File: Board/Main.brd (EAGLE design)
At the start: 43.2 x 30.5 mm, 1 part

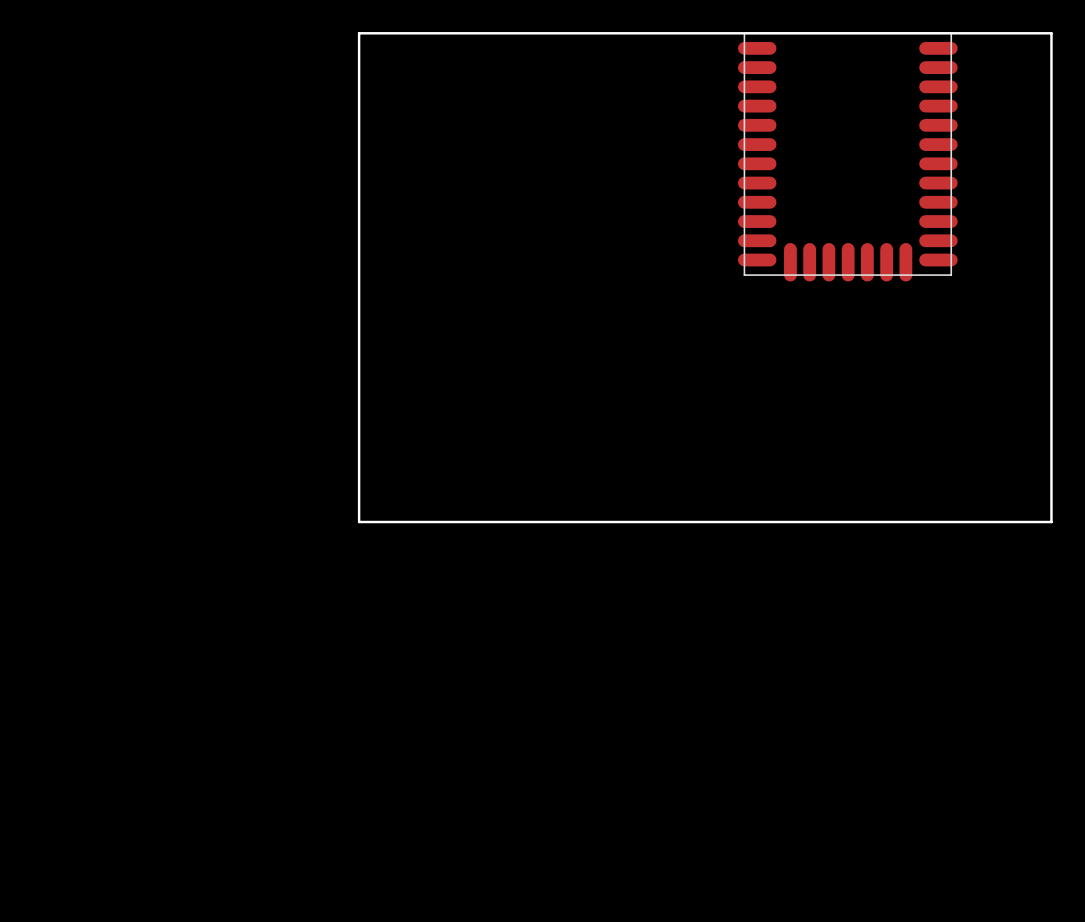
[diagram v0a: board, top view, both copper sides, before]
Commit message: Add battery managment
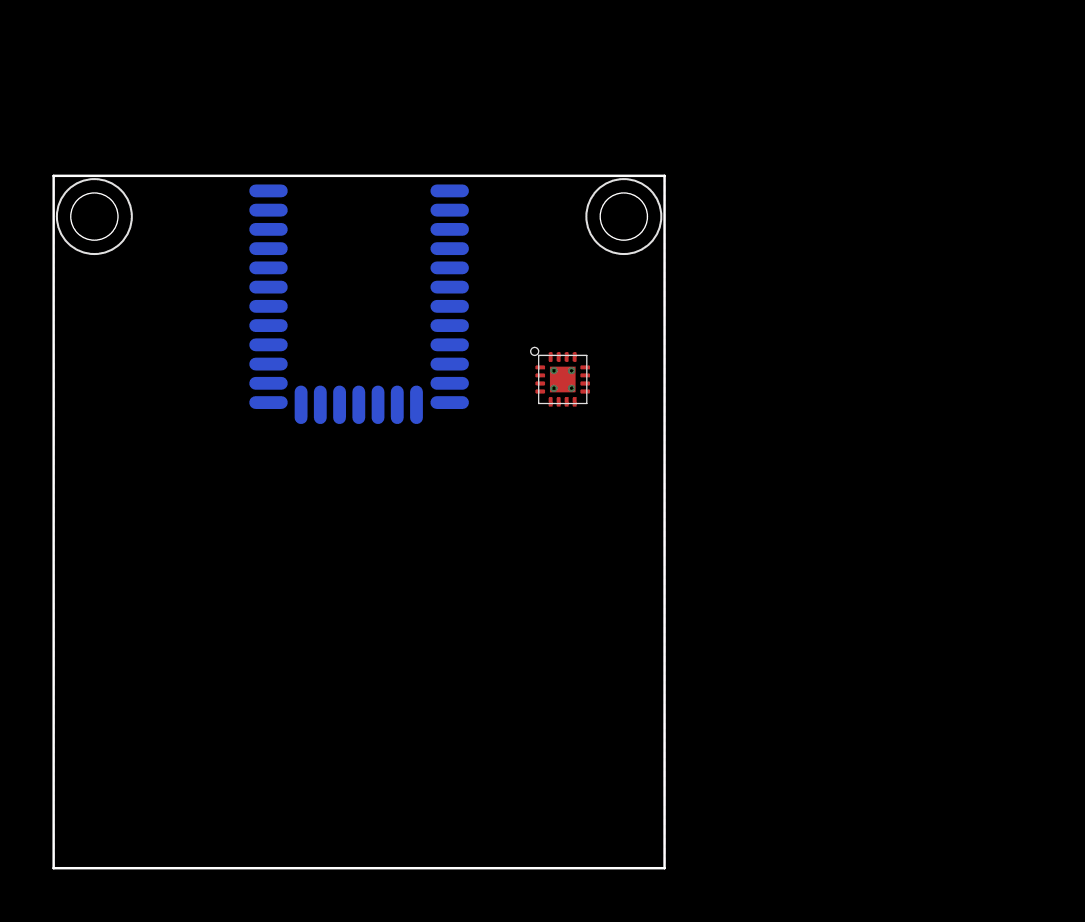
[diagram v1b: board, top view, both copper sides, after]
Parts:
- removed BGM111: BGM111, Main Components:BGM111
- added BLUETOOTH: BGM111, Main Components:BGM111
- added CHARGER: BQ24075, Main Components:VQFN-16
- added U$1, U$2: (no value), Hardware:#4_SCREW
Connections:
- new net +3V3: BLUETOOTH.VDD
- new net +5V0: CHARGER.13
- new net GND: BLUETOOTH.GND@0, BLUETOOTH.GND@1, BLUETOOTH.GND@2, BLUETOOTH.GND@3, CHARGER.15, CHARGER.17, CHARGER.17@1, CHARGER.17@2, CHARGER.17@3, CHARGER.17@4, CHARGER.4, CHARGER.8
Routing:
- added copper zone on layer 1, net GND
- added copper zone on layer 16, net GND
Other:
- board size 43.2 x 30.5 mm -> 38.1 x 43.2 mm
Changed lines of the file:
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@@
 <board>
 <plain>
-<wire x1="0" y1="0" x2="0" y2="30.48" width="0.1524" layer="20"/>
-<wire x1="0" y1="30.48" x2="43.18" y2="30.48" width="0.1524" layer="20"/>
-<wire x1="43.18" y1="30.48" x2="43.18" y2="0" width="0.1524" layer="20"/>
-<wire x1="43.18" y1="0" x2="0" y2="0" width="0.1524" layer="20"/>
+<wire x1="-19.05" y1="-21.59" x2="-19.05" y2="21.59" width="0.1524" layer="20"/>
+<wire x1="-19.05" y1="21.59" x2="19.05" y2="21.59" width="0.1524" layer="20"/>
+<wire x1="19.05" y1="21.59" x2="19.05" y2="-21.59" width="0.1524" layer="20"/>
+<wire x1="19.05" y1="-21.59" x2="-19.05" y2="-21.59" width="0.1524" layer="20"/>
 </plain>
 <attributes>
@@
 </class>
 </classes>
-<designrules name="default">
+<designrules name="OshPark *">
 <description language="de">&lt;b&gt;EAGLE Design Rules&lt;/b&gt;
 &lt;p&gt;
@@
 <param name="mdViaViaSameLayer" value="6mil"/>
 <param name="mnLayersViaInSmd" value="2"/>
-<param name="mdCopperDimension" value="40mil"/>
+<param name="mdCopperDimension" value="15mil"/>
 <param name="mdDrill" value="6mil"/>
 <param name="mdSmdStop" value="0mil"/>
 <param name="msWidth" value="6mil"/>
-<param name="msDrill" value="0.35mm"/>
-<param name="msMicroVia" value="9.99mm"/>
+<param name="msDrill" value="10mil"/>
+<param name="msMicroVia" value="10mil"/>
 <param name="msBlindViaRatio" value="0.5"/>
-<param name="rvPadTop" value="0.25"/>
-<param name="rvPadInner" value="0.25"/>
-<param name="rvPadBottom" value="0.25"/>
-<param name="rvViaOuter" value="0.25"/>
-<param name="rvViaInner" value="0.25"/>
+<param name="rvPadTop" value="0"/>
+<param name="rvPadInner" value="0"/>
+<param name="rvPadBottom" value="0"/>
+<param name="rvViaOuter" value="0"/>
+<param name="rvViaInner" value="0"/>
 <param name="rvMicroViaOuter" value="0.25"/>
 <param name="rvMicroViaInner" value="0.25"/>
-<param name="rlMinPadTop" value="10mil"/>
+<param name="rlMinPadTop" value="5mil"/>
 <param name="rlMaxPadTop" value="20mil"/>
-<param name="rlMinPadInner" value="10mil"/>
+<param name="rlMinPadInner" value="5mil"/>
 <param name="rlMaxPadInner" value="20mil"/>
-<param name="rlMinPadBottom" value="10mil"/>
+<param name="rlMinPadBottom" value="5mil"/>
 <param name="rlMaxPadBottom" value="20mil"/>
-<param name="rlMinViaOuter" value="8mil"/>
+<param name="rlMinViaOuter" value="5mil"/>
 <param name="rlMaxViaOuter" value="20mil"/>
-<param name="rlMinViaInner" value="8mil"/>
+<param name="rlMinViaInner" value="5mil"/>
 <param name="rlMaxViaInner" value="20mil"/>
 <param name="rlMinMicroViaOuter" value="4mil"/>
@@
 <param name="mvStopFrame" value="1"/>
 <param name="mvCreamFrame" value="0"/>
-<param name="mlMinStopFrame" value="4mil"/>
+<param name="mlMinStopFrame" value="2mil"/>
 <param name="mlMaxStopFrame" value="4mil"/>
 <param name="mlMinCreamFrame" value="0mil"/>
@@
 <param name="checkRestrict" value="1"/>
 <param name="checkStop" value="0"/>
-<param name="checkValues" value="0"/>
+<param name="checkValues" value="1"/>
 <param name="checkNames" value="1"/>
 <param name="checkWireStubs" value="1"/>
@@
 </autorouter>
 <elements>
-<element name="BGM111" library="Main Components" package="BGM111" value="BGM111" x="30.48" y="30.48" smashed="yes"/>
+<element name="CHARGER" library="Main Components" package="VQFN-16" value="BQ24075" x="12.7" y="8.89" smashed="yes">
+<attribute name="VALUE" value="BQ24075" x="12.7" y="8.89" size="1.778" layer="27" display="off"/>
+</element>
+<element name="BLUETOOTH" library="Main Components" package="BGM111" value="BGM111" x="0" y="21.59" smashed="yes" rot="MR0">
+<attribute name="NAME" x="1" y="13.59" size="1.27" layer="26" font="vector" rot="MR90" align="bottom-center"/>
+<attribute name="VALUE" x="-2" y="13.59" size="1.27" layer="28" font="vector" rot="MR90" align="bottom-center"/>
+</element>
+<element name="U$1" library="Hardware" package="#4_SCREW" value="" x="-16.51" y="19.05" smashed="yes"/>
+<element name="U$2" library="Hardware" package="#4_SCREW" value="" x="16.51" y="19.05" smashed="yes"/>
 </elements>
 <signals>
+<signal name="GND">
+<polygon width="0.1524" layer="1" isolate="0.4064">
+<vertex x="-19.05" y="21.59"/>
+<vertex x="19.05" y="21.59"/>
+<vertex x="19.05" y="-21.59"/>
+<vertex x="-19.05" y="-21.59"/>
+</polygon>
+<polygon width="0.1524" layer="16" isolate="0.4064">
+<vertex x="-19.05" y="21.59"/>
+<vertex x="19.05" y="21.59"/>
+<vertex x="19.05" y="-21.59"/>
+<vertex x="-19.05" y="-21.59"/>
+</polygon>
+<contactref element="BLUETOOTH" pad="GND@1"/>
+<contactref element="BLUETOOTH" pad="GND@3"/>
+<contactref element="BLUETOOTH" pad="GND@0"/>
+<contactref element="BLUETOOTH" pad="GND@2"/>
+<contactref element="CHARGER" pad="17@1"/>
+<contactref element="CHARGER" pad="8"/>
+<contactref element="CHARGER" pad="17@4"/>
+<contactref element="CHARGER" pad="17@3"/>
+<contactref element="CHARGER" pad="17"/>
+<contactref element="CHARGER" pad="17@2"/>
+<contactref element="CHARGER" pad="4"/>
+<contactref element="CHARGER" pad="15"/>
+<wire x1="12.15" y1="8.34" x2="12.7" y2="8.89" width="0" layer="19" extent="1-1"/>
+<wire x1="11.3" y1="8.14" x2="12.15" y2="8.34" width="0" layer="19" extent="1-1"/>
+<wire x1="13.45" y1="7.49" x2="13.25" y2="8.34" width="0" layer="19" extent="1-1"/>
+<wire x1="12.45" y1="10.29" x2="12.15" y2="9.44" width="0" layer="19" extent="1-1"/>
+</signal>
+<signal name="+3V3">
+<contactref element="BLUETOOTH" pad="VDD"/>
+</signal>
+<signal name="+5V0">
+<contactref element="CHARGER" pad="13"/>
+</signal>
 </signals>
 <mfgpreviewcolors>

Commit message: Add motor driver
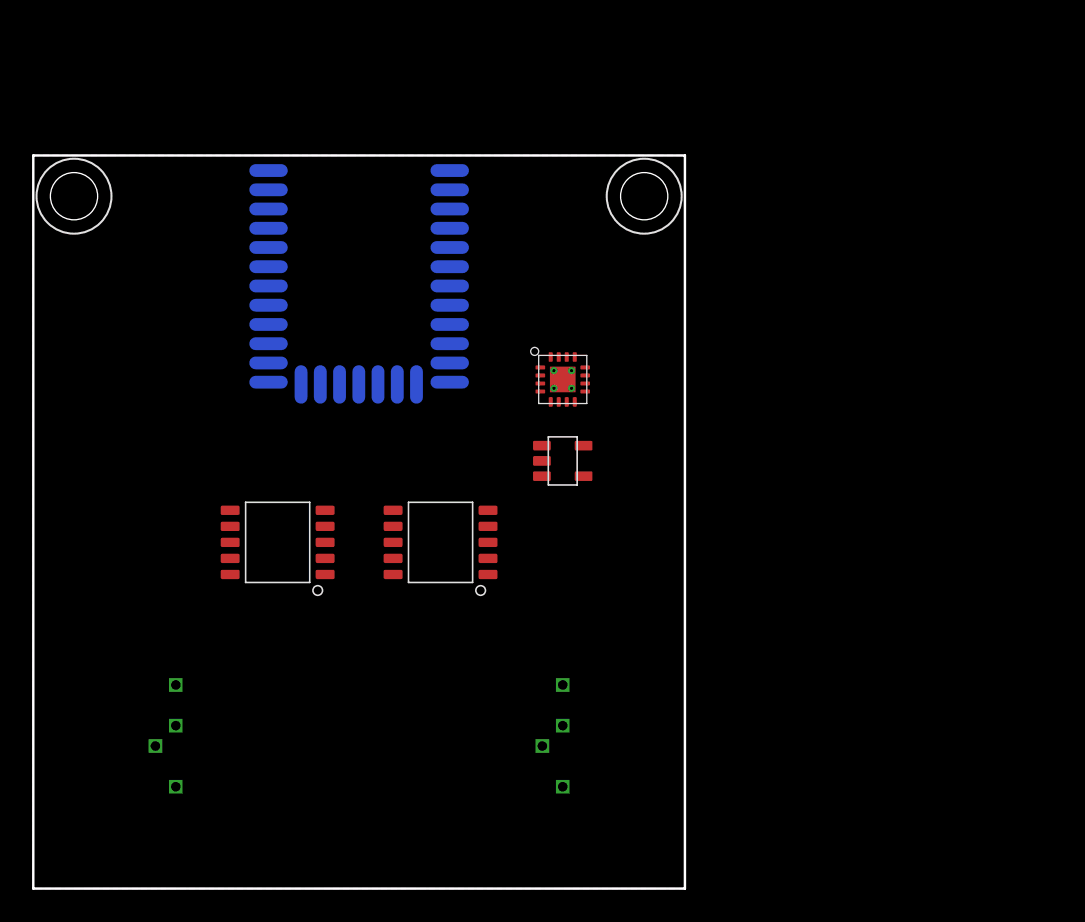
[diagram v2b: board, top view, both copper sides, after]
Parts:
- added M1, M2: LB1909MC, Components:SOIC-10
- added REGULATOR: TLV755P, Components:SOT-23-5
- added U$3, U$4: MOTOR, Components:MOTOR
- moved U$1 1.80 mm to (-17.8, 20.3)
- moved U$2 1.80 mm to (17.8, 20.3)
- moved BLUETOOTH 1.27 mm to (0.00, 22.9)
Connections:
- new net N$1: CHARGER.10, CHARGER.11, REGULATOR.1, REGULATOR.3
- new net N$2: M1.7, U$4.P$2
- new net N$3: M2.7, U$3.P$2
- new net N$4: M2.8, U$3.P$1
- new net N$5: M1.8, U$4.P$1
- new net N$6: M1.9, U$4.P$3
- new net N$7: M1.10, U$4.P$4
- new net N$8: M2.9, U$3.P$3
- new net N$9: M2.10, U$3.P$4
- net +3V3: now also M1.1, M2.1, REGULATOR.5
- net GND: now also M1.6, M2.6, REGULATOR.2
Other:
- board size 38.1 x 43.2 mm -> 40.6 x 45.7 mm
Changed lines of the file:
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@@
 <board>
 <plain>
-<wire x1="-19.05" y1="-21.59" x2="-19.05" y2="21.59" width="0.1524" layer="20"/>
-<wire x1="-19.05" y1="21.59" x2="19.05" y2="21.59" width="0.1524" layer="20"/>
-<wire x1="19.05" y1="21.59" x2="19.05" y2="-21.59" width="0.1524" layer="20"/>
-<wire x1="19.05" y1="-21.59" x2="-19.05" y2="-21.59" width="0.1524" layer="20"/>
+<wire x1="-20.32" y1="-22.86" x2="-20.32" y2="22.86" width="0.1524" layer="20"/>
+<wire x1="-20.32" y1="22.86" x2="20.32" y2="22.86" width="0.1524" layer="20"/>
+<wire x1="20.32" y1="22.86" x2="20.32" y2="-22.86" width="0.1524" layer="20"/>
+<wire x1="20.32" y1="-22.86" x2="-20.32" y2="-22.86" width="0.1524" layer="20"/>
 </plain>
 <attributes>
@@
 <attribute name="VALUE" value="BQ24075" x="12.7" y="8.89" size="1.778" layer="27" display="off"/>
 </element>
-<element name="BLUETOOTH" library="Main Components" package="BGM111" value="BGM111" x="0" y="21.59" smashed="yes" rot="MR0">
-<attribute name="NAME" x="1" y="13.59" size="1.27" layer="26" font="vector" rot="MR90" align="bottom-center"/>
-<attribute name="VALUE" x="-2" y="13.59" size="1.27" layer="28" font="vector" rot="MR90" align="bottom-center"/>
+<element name="BLUETOOTH" library="Main Components" package="BGM111" value="BGM111" x="0" y="22.86" smashed="yes" rot="MR0">
+<attribute name="NAME" x="1" y="14.86" size="1.27" layer="26" font="vector" rot="MR90" align="bottom-center"/>
+<attribute name="VALUE" x="-2" y="14.86" size="1.27" layer="28" font="vector" rot="MR90" align="bottom-center"/>
 </element>
-<element name="U$1" library="Hardware" package="#4_SCREW" value="" x="-16.51" y="19.05" smashed="yes"/>
-<element name="U$2" library="Hardware" package="#4_SCREW" value="" x="16.51" y="19.05" smashed="yes"/>
+<element name="U$1" library="Hardware" package="#4_SCREW" value="" x="-17.78" y="20.32" smashed="yes"/>
+<element name="U$2" library="Hardware" package="#4_SCREW" value="" x="17.78" y="20.32" smashed="yes"/>
+<element name="REGULATOR" library="Components" package="SOT-23-5" value="TLV755P" x="12.7" y="3.81" smashed="yes"/>
+<element name="M1" library="Components" package="SOIC-10" value="LB1909MC" x="-5.08" y="-1.27" smashed="yes" rot="R180"/>
+<element name="M2" library="Components" package="SOIC-10" value="LB1909MC" x="5.08" y="-1.27" smashed="yes" rot="R180"/>
+<element name="U$3" library="Components" package="MOTOR" value="MOTOR" x="12.7" y="-12.7" smashed="yes" rot="R90"/>
+<element name="U$4" library="Components" package="MOTOR" value="MOTOR" x="-11.43" y="-12.7" smashed="yes" rot="R90"/>
 </elements>
 <signals>
 <signal name="GND">
 <polygon width="0.1524" layer="1" isolate="0.4064">
-<vertex x="-19.05" y="21.59"/>
-<vertex x="19.05" y="21.59"/>
-<vertex x="19.05" y="-21.59"/>
-<vertex x="-19.05" y="-21.59"/>
+<vertex x="-20.32" y="22.86"/>
+<vertex x="20.32" y="22.86"/>
+<vertex x="20.32" y="-22.86"/>
+<vertex x="-20.32" y="-22.86"/>
 </polygon>
 <polygon width="0.1524" layer="16" isolate="0.4064">
-<vertex x="-19.05" y="21.59"/>
-<vertex x="19.05" y="21.59"/>
-<vertex x="19.05" y="-21.59"/>
-<vertex x="-19.05" y="-21.59"/>
+<vertex x="-20.32" y="22.86"/>
+<vertex x="20.32" y="22.86"/>
+<vertex x="20.32" y="-22.86"/>
+<vertex x="-20.32" y="-22.86"/>
 </polygon>
 <contactref element="BLUETOOTH" pad="GND@1"/>
@@
 <contactref element="CHARGER" pad="4"/>
 <contactref element="CHARGER" pad="15"/>
+<contactref element="REGULATOR" pad="2"/>
+<contactref element="M1" pad="6"/>
+<contactref element="M2" pad="6"/>
 <wire x1="12.15" y1="8.34" x2="12.7" y2="8.89" width="0" layer="19" extent="1-1"/>
 <wire x1="11.3" y1="8.14" x2="12.15" y2="8.34" width="0" layer="19" extent="1-1"/>
-<wire x1="13.45" y1="7.49" x2="13.25" y2="8.34" width="0" layer="19" extent="1-1"/>
 <wire x1="12.45" y1="10.29" x2="12.15" y2="9.44" width="0" layer="19" extent="1-1"/>
 </signal>
 <signal name="+3V3">
 <contactref element="BLUETOOTH" pad="VDD"/>
+<contactref element="REGULATOR" pad="5"/>
+<contactref element="M1" pad="1"/>
+<contactref element="M2" pad="1"/>
+<wire x1="8.04" y1="-3.27" x2="14" y2="4.76" width="0" layer="19" extent="1-1"/>
+<wire x1="-2.12" y1="-3.27" x2="8.04" y2="-3.27" width="0" layer="19" extent="1-1"/>
+<wire x1="-5.65" y1="19.52" x2="-2.12" y2="-3.27" width="0" layer="19" extent="1-16"/>
 </signal>
 <signal name="+5V0">
 <contactref element="CHARGER" pad="13"/>
 </signal>
+<signal name="N$1">
+<contactref element="REGULATOR" pad="1"/>
+<contactref element="REGULATOR" pad="3"/>
+<contactref element="CHARGER" pad="10"/>
+<contactref element="CHARGER" pad="11"/>
+<wire x1="14.1" y1="9.14" x2="14.1" y2="8.64" width="0" layer="19" extent="1-1"/>
+<wire x1="11.4" y1="4.76" x2="14.1" y2="8.64" width="0" layer="19" extent="1-1"/>
+<wire x1="11.4" y1="2.86" x2="11.4" y2="4.76" width="0" layer="19" extent="1-1"/>
+</signal>
+<signal name="N$2">
+<contactref element="M1" pad="7"/>
+<contactref element="U$4" pad="P$2"/>
+<wire x1="-8.04" y1="-0.27" x2="-12.7" y2="-13.97" width="0" layer="19" extent="1-1"/>
+</signal>
+<signal name="N$3">
+<contactref element="M2" pad="7"/>
+<contactref element="U$3" pad="P$2"/>
+<wire x1="2.12" y1="-0.27" x2="11.43" y2="-13.97" width="0" layer="19" extent="1-1"/>
+</signal>
+<signal name="N$4">
+<contactref element="M2" pad="8"/>
+<contactref element="U$3" pad="P$1"/>
+<wire x1="2.12" y1="-1.27" x2="12.7" y2="-16.51" width="0" layer="19" extent="1-1"/>
+</signal>
+<signal name="N$5">
+<contactref element="M1" pad="8"/>
+<contactref element="U$4" pad="P$1"/>
+<wire x1="-8.04" y1="-1.27" x2="-11.43" y2="-16.51" width="0" layer="19" extent="1-1"/>
+</signal>
+<signal name="N$6">
+<contactref element="U$4" pad="P$3"/>
+<contactref element="M1" pad="9"/>
+<wire x1="-8.04" y1="-2.27" x2="-11.43" y2="-12.7" width="0" layer="19" extent="1-1"/>
+</signal>
+<signal name="N$7">
+<contactref element="M1" pad="10"/>
+<contactref element="U$4" pad="P$4"/>
+<wire x1="-8.04" y1="-3.27" x2="-11.43" y2="-10.16" width="0" layer="19" extent="1-1"/>
+</signal>
+<signal name="N$8">
+<contactref element="M2" pad="9"/>
+<contactref element="U$3" pad="P$3"/>
+<wire x1="12.7" y1="-12.7" x2="2.12" y2="-2.27" width="0" layer="19" extent="1-1"/>
+</signal>
+<signal name="N$9">
+<contactref element="M2" pad="10"/>
+<contactref element="U$3" pad="P$4"/>
+<wire x1="12.7" y1="-10.16" x2="2.12" y2="-3.27" width="0" layer="19" extent="1-1"/>
+</signal>
 </signals>
